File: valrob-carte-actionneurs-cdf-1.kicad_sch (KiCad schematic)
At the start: 99 parts, among them J1 USB_C_Receptacle_USB2.0_14P, J2 Conn_01x02, J3 Conn_01x02, J4 Conn_01x04_Pin, M1 Motor_Servo, M10 Motor_Servo, M11 Motor_Servo, M12 Motor_Servo, M13 Motor_Servo, M14 Motor_Servo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

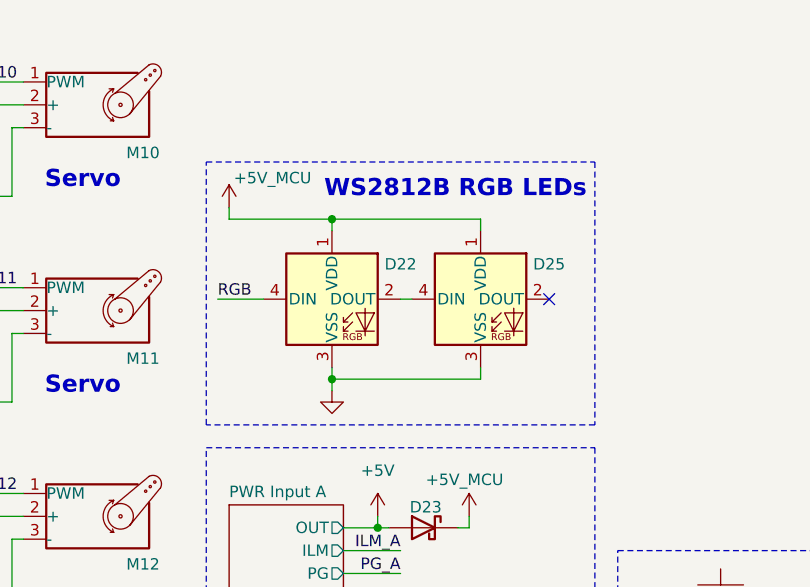
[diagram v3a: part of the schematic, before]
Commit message: schem: remove one rgb led
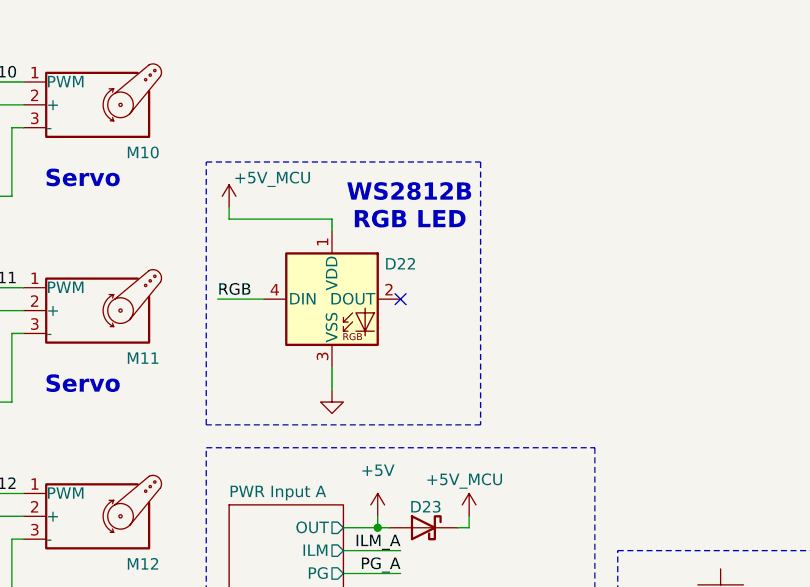
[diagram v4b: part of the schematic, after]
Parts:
- removed D25: WS2812B, LED_SMD:LED_WS2812B_PLCC4_5.0x5.0mm_P3.2mm, symbol LED:WS2812B
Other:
- note added: "WS2812B RGB LED"
- note removed: "WS2812B RGB LEDs"
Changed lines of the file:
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@@
 	(rectangle
 		(start 86.36 93.98)
-		(end 129.54 123.19)
+		(end 116.84 123.19)
 		(stroke
 			(width 0)
@@
 		)
 	)
-	(text "WS2812B RGB LEDs"
+	(text "WS2812B\nRGB LED"
 		(exclude_from_sim no)
-		(at 114.046 97.028 0)
+		(at 108.966 99.06 0)
 		(effects
 			(font
@@
 	)
 	(junction
-		(at 100.33 118.11)
-		(diameter 0)
-		(color 0 0 0 0)
-	)
-	(junction
 		(at 22.86 120.65)
 		(diameter 0)
@@
 	)
 	(junction
-		(at 100.33 100.33)
-		(diameter 0)
-		(color 0 0 0 0)
-	)
-	(junction
 		(at 135.89 148.59)
 		(diameter 0)
@@
 	)
 	(no_connect
+		(at 107.95 109.22)
+	)
+	(no_connect
 		(at 248.92 125.73)
 	)
@@
 	)
 	(no_connect
-		(at 124.46 109.22)
-	)
-	(no_connect
 		(at 248.92 123.19)
 	)
@@
 	(wire
 		(pts
-			(xy 107.95 109.22) (xy 109.22 109.22)
-		)
-		(stroke
-			(width 0)
-			(type default)
-		)
-	)
-	(wire
-		(pts
 			(xy 143.51 34.29) (xy 143.51 36.83)
 		)
@@
 	(wire
 		(pts
-			(xy 100.33 118.11) (xy 100.33 119.38)
-		)
-		(stroke
-			(width 0)
-			(type default)
-		)
-	)
-	(wire
-		(pts
 			(xy 31.75 67.31) (xy 30.48 67.31)
 		)
@@
 	(wire
 		(pts
-			(xy 100.33 116.84) (xy 100.33 118.11)
+			(xy 100.33 116.84) (xy 100.33 119.38)
 		)
 		(stroke
@@
 	(wire
 		(pts
-			(xy 116.84 100.33) (xy 116.84 101.6)
-		)
-		(stroke
-			(width 0)
-			(type default)
-		)
-	)
-	(wire
-		(pts
 			(xy 26.67 143.51) (xy 26.67 144.78)
 		)
@@
 	(wire
 		(pts
-			(xy 100.33 118.11) (xy 116.84 118.11)
-		)
-		(stroke
-			(width 0)
-			(type default)
-		)
-	)
-	(wire
-		(pts
 			(xy 234.95 146.05) (xy 234.95 147.32)
 		)
@@
 	(wire
 		(pts
-			(xy 100.33 100.33) (xy 116.84 100.33)
-		)
-		(stroke
-			(width 0)
-			(type default)
-		)
-	)
-	(wire
-		(pts
 			(xy 41.91 185.42) (xy 40.64 185.42)
 		)
@@
 	(wire
 		(pts
-			(xy 116.84 116.84) (xy 116.84 118.11)
-		)
-		(stroke
-			(width 0)
-			(type default)
-		)
-	)
-	(wire
-		(pts
 			(xy 99.06 44.45) (xy 99.06 52.07)
 		)
@@
 					(unit 1)
 				)
-			)
-		)
-	)
-	(symbol
-		(lib_id "LED:WS2812B")
-		(at 116.84 109.22 0)
-		(unit 1)
-		(exclude_from_sim no)
-		(in_bom yes)
-		(on_board yes)
-		(dnp no)
-		(fields_autoplaced yes)
-		(property "Reference" "D25"
-			(at 124.46 105.3398 0)
-			(effects
-				(font
-					(size 1.27 1.27)
-				)
-			)
-		)
-		(property "Value" "WS2812B"
-			(at 128.27 105.3398 0)
-			(effects
-				(font
-					(size 1.27 1.27)
-				)
-				(hide yes)
-			)
-		)
-		(property "Footprint" "LED_SMD:LED_WS2812B_PLCC4_5.0x5.0mm_P3.2mm"
-			(at 118.11 116.84 0)
-			(effects
-				(font
-					(size 1.27 1.27)
-				)
-				(justify left top)
-				(hide yes)
-			)
-		)
-		(property "Datasheet" "https://cdn-shop.adafruit.com/datasheets/WS2812B.pdf"
-			(at 119.38 118.745 0)
-			(effects
-				(font
-					(size 1.27 1.27)
-				)
-				(justify left top)
-				(hide yes)
-			)
-		)
-		(property "Description" "RGB LED with integrated controller"
-			(at 116.84 109.22 0)
-			(effects
-				(font
-					(size 1.27 1.27)
-				)
-				(hide yes)
-			)
-		)
-		(property "Basic" "Z"
-			(at 116.84 109.22 0)
-			(effects
-				(font
-					(size 1.27 1.27)
-				)
-				(hide yes)
-			)
-		)
-		(property "JLCPCB Part #" "C2874885"
-			(at 116.84 109.22 0)
-			(effects
-				(font
-					(size 1.27 1.27)
-				)
-				(hide yes)
-			)
-		)
-		(property "Manufacturer" "Worldsemi"
-			(at 116.84 109.22 0)
-			(effects
-				(font
-					(size 1.27 1.27)
-				)
-				(hide yes)
-			)
-		)
-		(property "Manufacturer Part Number" "WS2812B-V5/W"
-			(at 116.84 109.22 0)
-			(effects
-				(font
-					(size 1.27 1.27)
-				)
-				(hide yes)
-			)
-		)
-		(pin "4"
-		)
-		(pin "1"
-		)
-		(pin "2"
-		)
-		(pin "3"
-		)
-		(instances
-			(project "valrob-carte-actionneurs-cdf-1"
-				(path "/6d04427e-e45e-4b7f-8323-501f87acc543"
-					(reference "D25")
-					(unit 1)
-				)

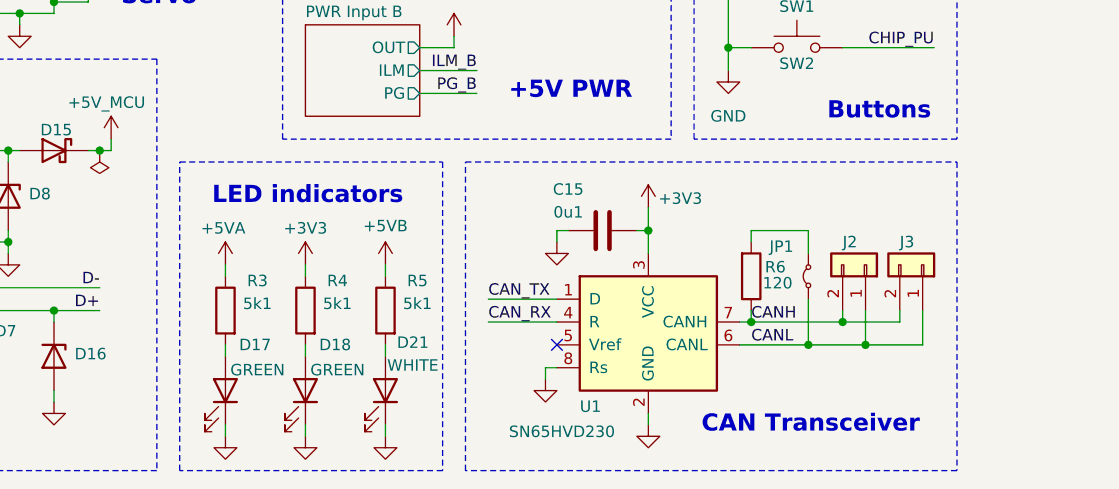
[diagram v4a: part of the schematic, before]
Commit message: schem: remove extra power indicator led
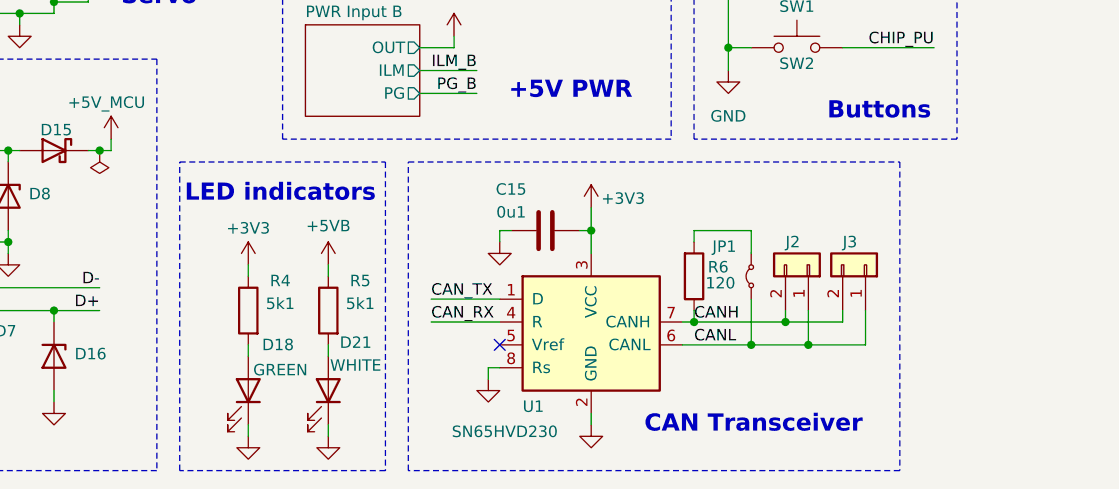
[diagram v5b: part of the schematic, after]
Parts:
- removed D17: GREEN, LED_SMD:LED_0805_2012Metric, symbol Device:LED
- removed R3: 5k1, Resistor_SMD:R_0402_1005Metric, symbol Device:R
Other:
- moved on the sheet: C15, D18, D21, J2, J3, JP1, R4, R5, R6, U1

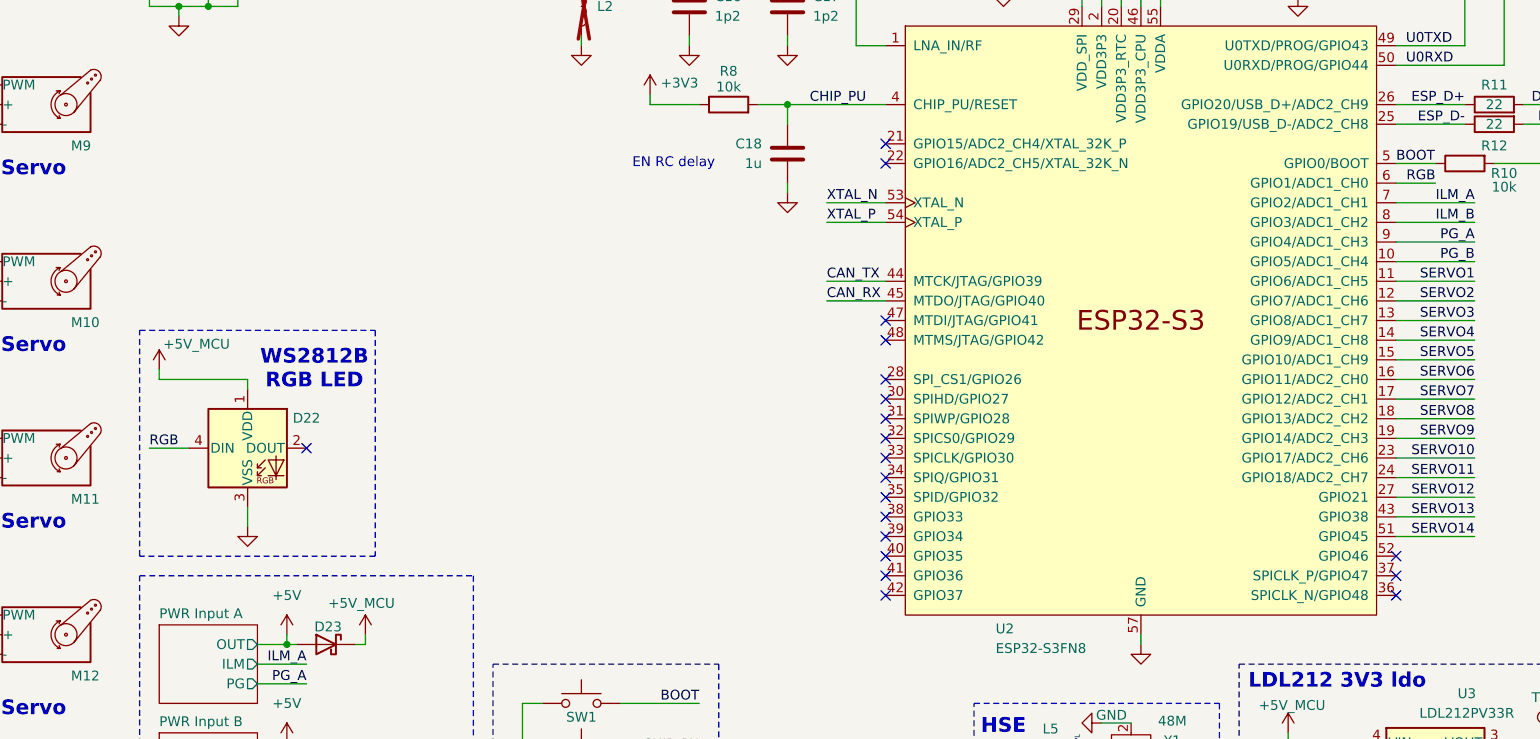
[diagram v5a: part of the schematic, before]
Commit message: schem: add mounting holes
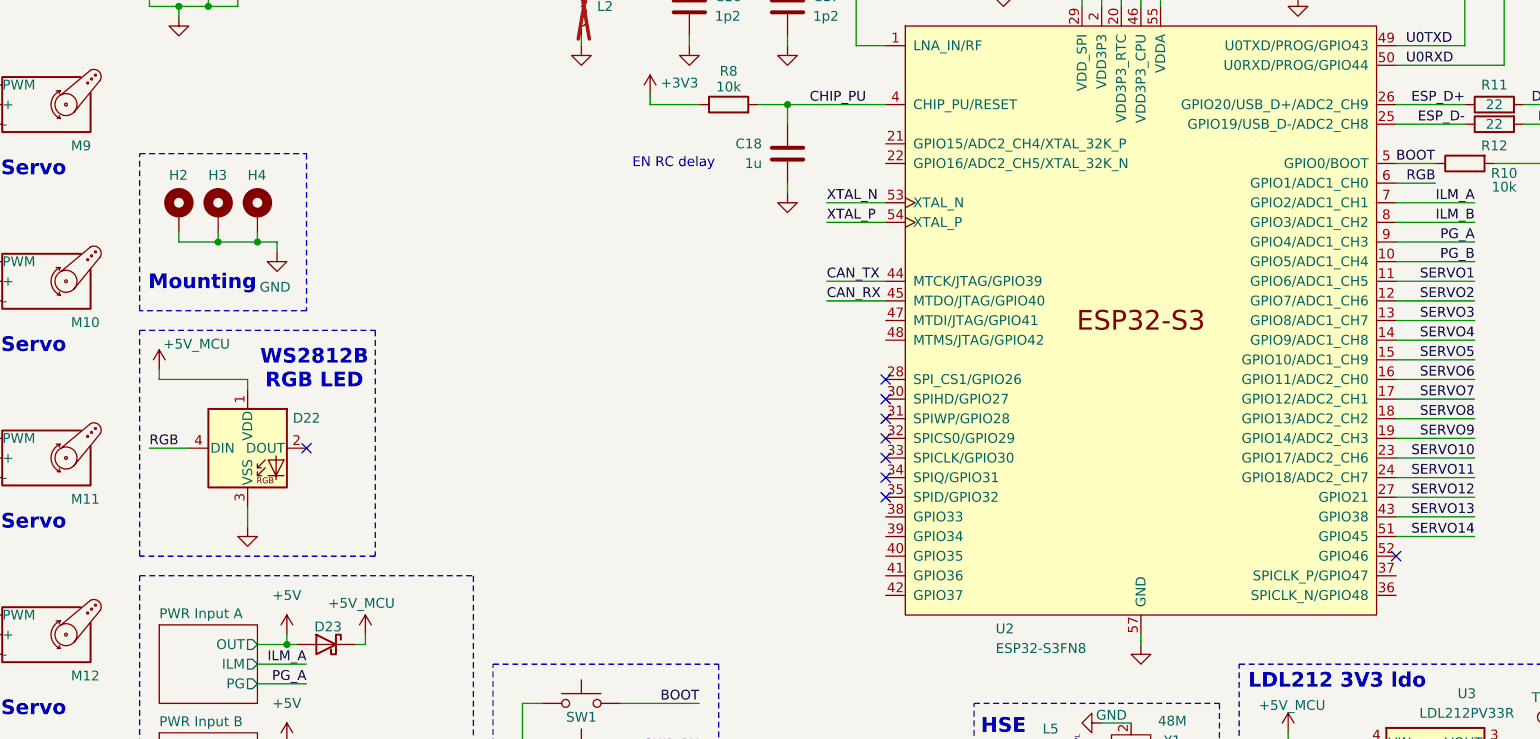
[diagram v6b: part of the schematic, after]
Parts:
- added H2, H3, H4: MountingHole_Pad, MountingHole:MountingHole_2.2mm_M2_Pad_Via, symbol Mechanical:MountingHole_Pad
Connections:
- net GND: now also H2.1, H3.1, H4.1
- no-connect marks 21 -> 10
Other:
- note added: "Mounting"

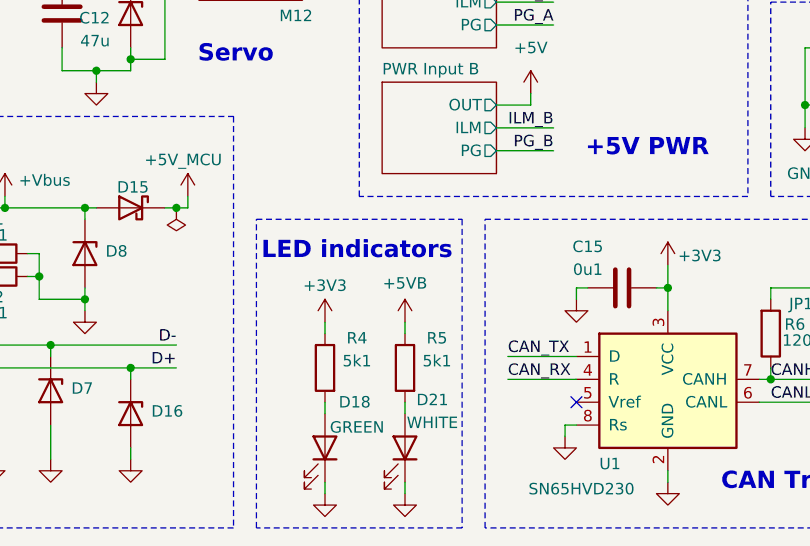
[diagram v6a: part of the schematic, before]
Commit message: pcb: add initial component placement
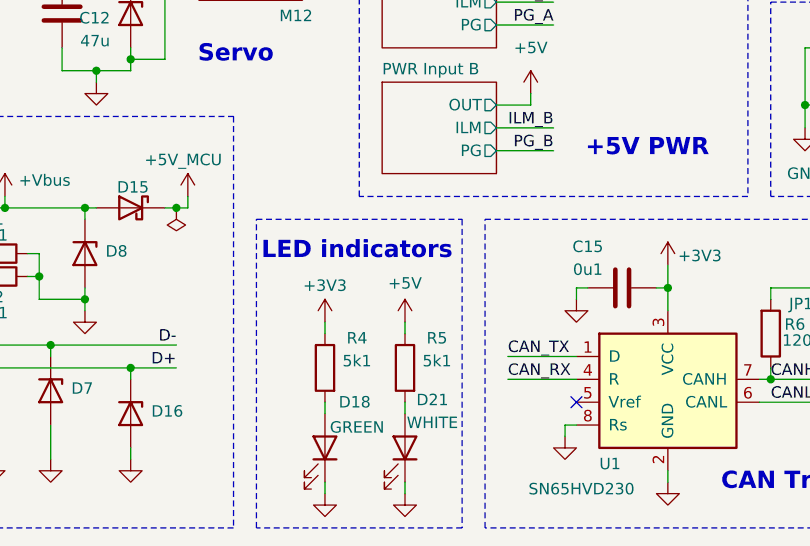
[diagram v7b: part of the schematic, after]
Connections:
- net +5VB is gone; now on net +5V: R5.1
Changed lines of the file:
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@@
 			)
 		)
-		(property "Value" "+5VB"
+		(property "Value" "+5V"
 			(at 91.44 168.402 0)
 			(effects
